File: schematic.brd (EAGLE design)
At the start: 100 x 70 mm, 33 parts, among them U1 ADP3338AKCZ-3.3RL7

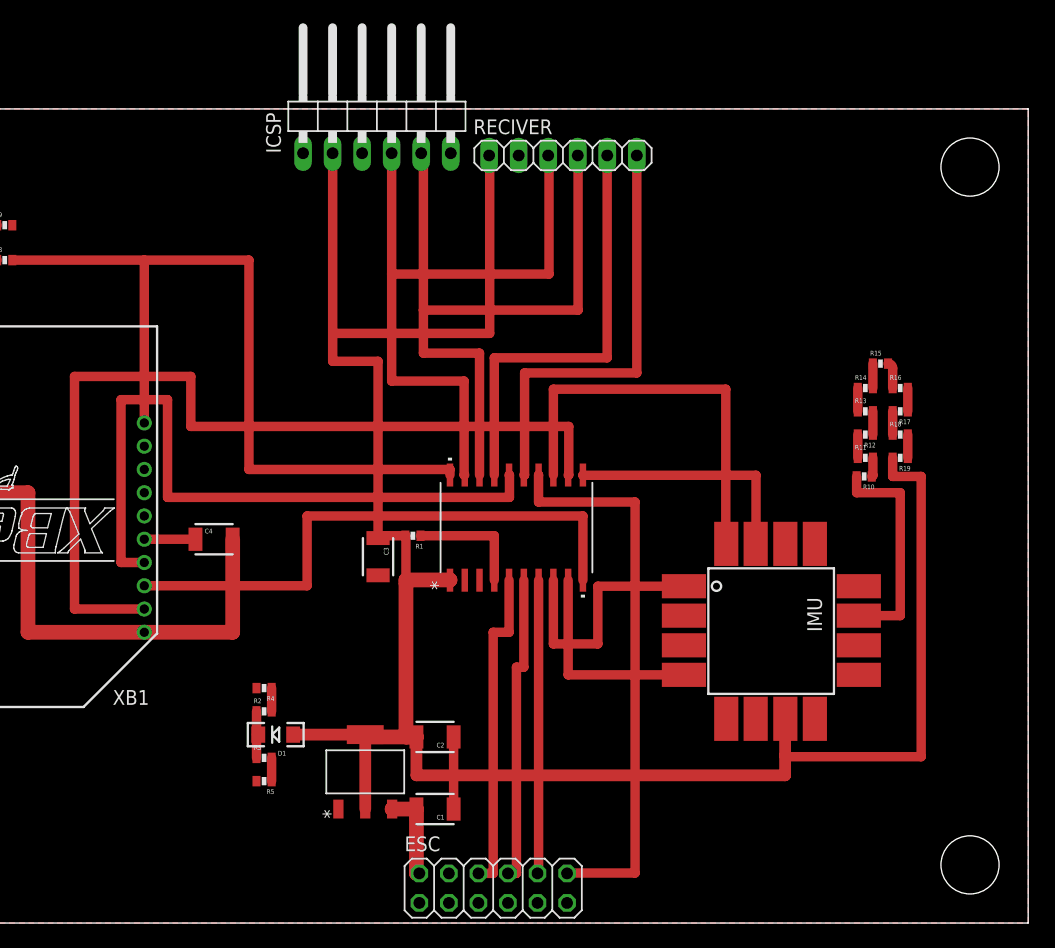
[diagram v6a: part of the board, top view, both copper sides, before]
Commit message: Added several missing components, rearanged some components to make routing easier and added last jumper cables. Board layout is theretically done now
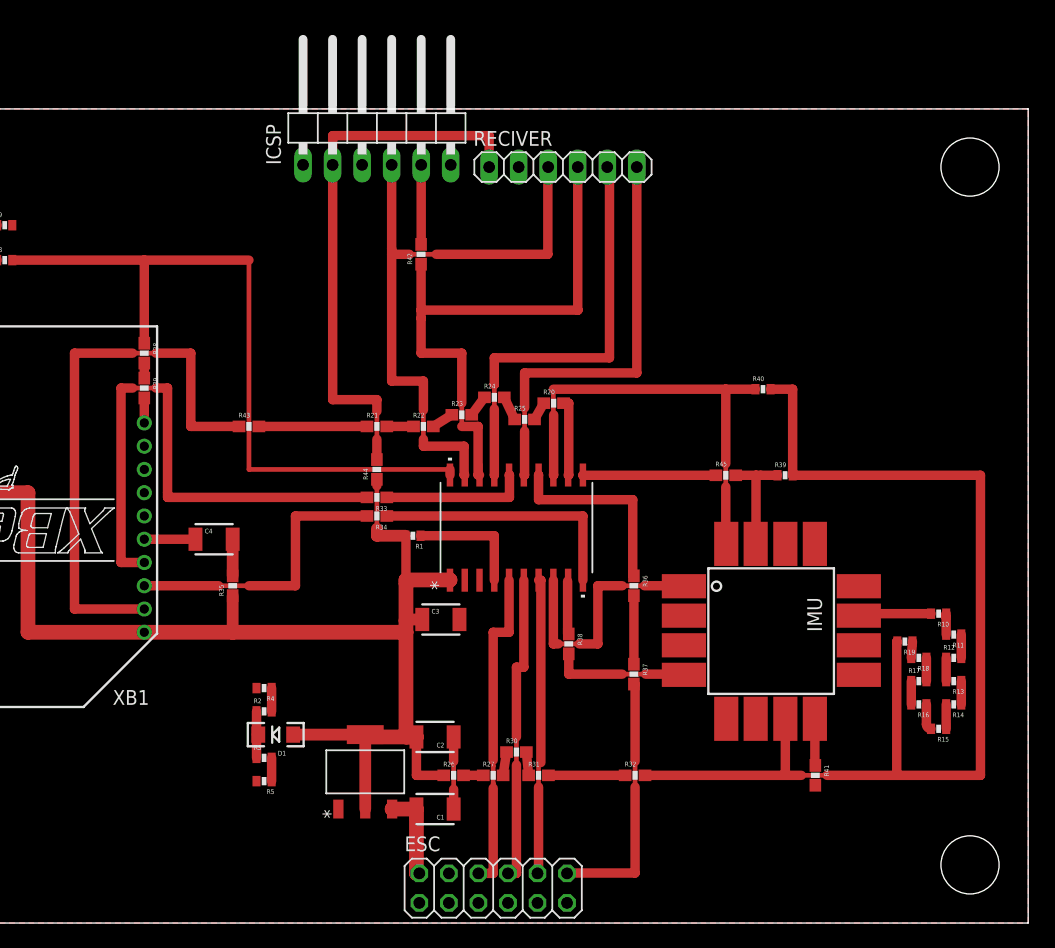
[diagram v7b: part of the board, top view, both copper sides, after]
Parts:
- added R20, R21, R22, R23, R24, R25, R26, R27, R28, R29, R30, R31, R32, R33, R34, R35, R36, R37, R38, R41, R42, R43, R44, R45: 0, SparkFun-Passives:0603-RES
- added R39, R40: 10k, SparkFun-Passives:0402-RES
- moved R15 31.8 mm to (92.3, 16.7), turned to 180 degrees
- moved R14 28.2 mm to (93.6, 18.8), turned to 180 degrees
- moved R16 27.2 mm to (90.6, 18.8), turned to 180 degrees
- moved R13 24.4 mm to (93.6, 20.8), turned to 180 degrees
- moved R17 23.3 mm to (90.6, 20.8), turned to 0 degrees
- moved R12 20.6 mm to (93.6, 22.8), turned to 0 degrees
- moved R18 19.3 mm to (90.6, 22.8), turned to 180 degrees
- moved R11 17.0 mm to (93.6, 24.8), turned to 180 degrees
- moved R19 15.8 mm to (89.4, 24.2)
- moved R10 13.4 mm to (92.3, 26.6)
- moved C3 7.64 mm to (49.5, 26.1), turned to 0 degrees
- moved ICSP 1.00 mm to (44.0, 69.0)
- moved RECIVER 1.00 mm to (60.0, 65.0)
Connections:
- removed net VCC: C4.2, XB1.1, XB1.14
- new net GND_S: R29.2, XB1.10
- new net N$1: R20.1, R25.2
- new net N$20: R21.2, R22.1
- new net N$21: R22.2, R23.1
- new net N$22: R23.2, R24.1
- new net N$23: R24.2, R25.1
- new net N$24: R28.2, R29.1
- new net N$25: MAIN_CONTROLLER.16, R33.1
- new net N$26: R26.2, R27.1
- new net N$27: R27.2, R30.1
- new net N$28: R30.2, R31.1
- new net N$29: R31.2, R32.1
- new net N$30: R34.2, XB1.3
- new net N$31: C4.2, R35.2
- new net N$32: MAIN_CONTROLLER.14, R36.1
- new net N$33: R36.2, R37.1
- new net N$34: IMU.P$4, R38.2
- new net N$35: IMU.P$8, R41.1
- new net N$36: R21.1, R43.2
- new net N$37: ICSP.5, R42.2
- new net N$38: ICSP.2, R44.2, RECIVER.1
- new net N$39: MAIN_CONTROLLER.11, R45.1
- new net RX_S: MAIN_CONTROLLER.12, R20.2
- new net VDD_S: IMU.P$7, R19.2, R32.2, R39.2, R40.2
- net GND: now also R28.1, R41.2; no longer IMU.P$8, XB1.10
- net IMU_INT: now also R38.1; no longer IMU.P$4
- net M4: now also R37.2; no longer MAIN_CONTROLLER.14
- net PGC/ROLL: now also R42.1; no longer ICSP.5
- net RX: now also R43.1; no longer MAIN_CONTROLLER.12
- net SCL: now also R39.1, R45.2; no longer MAIN_CONTROLLER.11
- net SDA: now also R40.1
- net TX: now also R34.1; no longer XB1.3
- net VDD: now also R26.1, R35.1, R44.1, XB1.1, XB1.14; no longer ICSP.2, IMU.P$7, R19.2, RECIVER.1
- net XBEE_INT: now also R33.2; no longer MAIN_CONTROLLER.16
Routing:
- net VDD_S: track 0.00 -> 96.5 mm
- net VDD: track 187.6 -> 113.5 mm
- net VCC: track 49.6 -> 0.00 mm
- net N$38: track 0.00 -> 47.8 mm
- net RX: track 77.0 -> 48.4 mm
- net TX: track 49.2 -> 22.4 mm
- net M4: track 48.4 -> 22.2 mm
- net N$30: track 0.00 -> 25.1 mm
- net N$32: track 0.00 -> 16.9 mm
- net IMU_INT: track 18.1 -> 4.65 mm
- net N$10: track 19.3 -> 6.38 mm
- net N$25: track 0.00 -> 12.5 mm
- net XBEE_INT: track 59.8 -> 47.5 mm
- net N$34: track 0.00 -> 11.7 mm
- net N$39: track 0.00 -> 11.5 mm
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
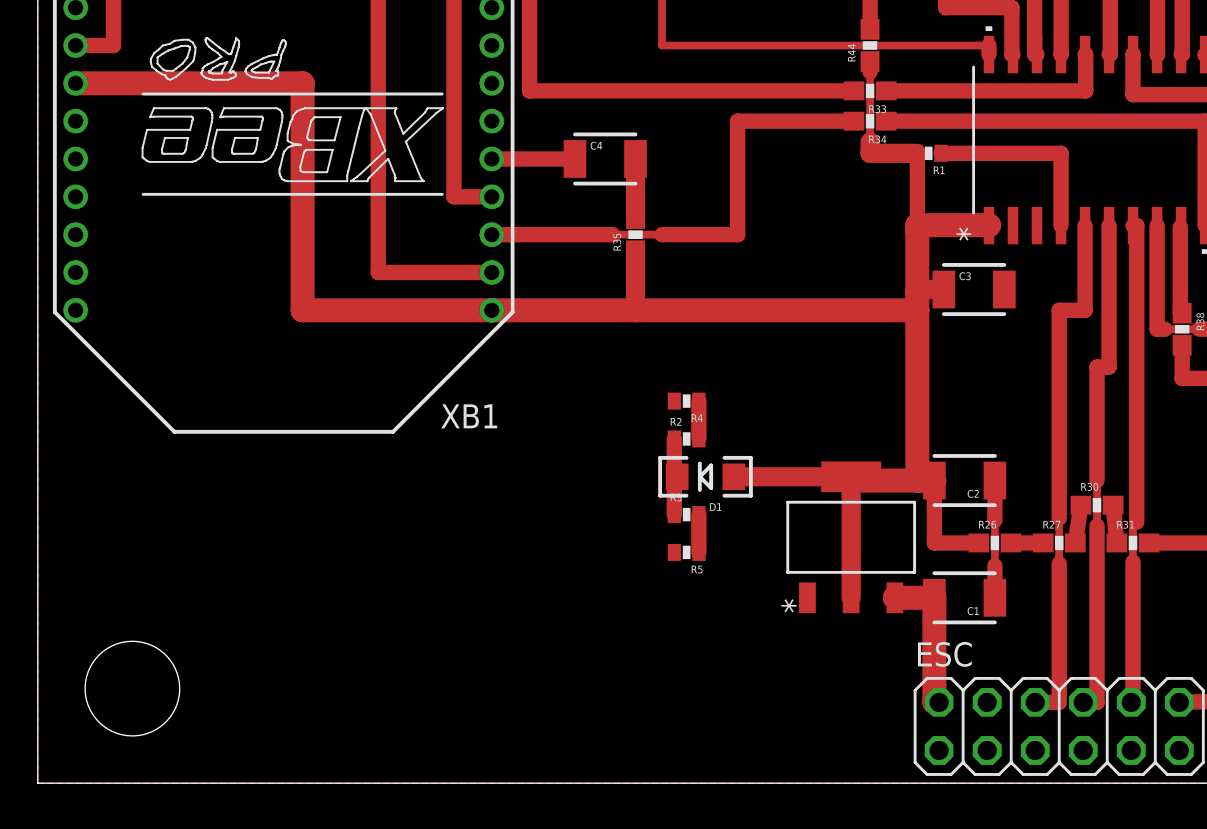
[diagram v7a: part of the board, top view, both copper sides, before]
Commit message: Rearanged several components to remove some jumper cables, added led's to unused pins on xbee and controller
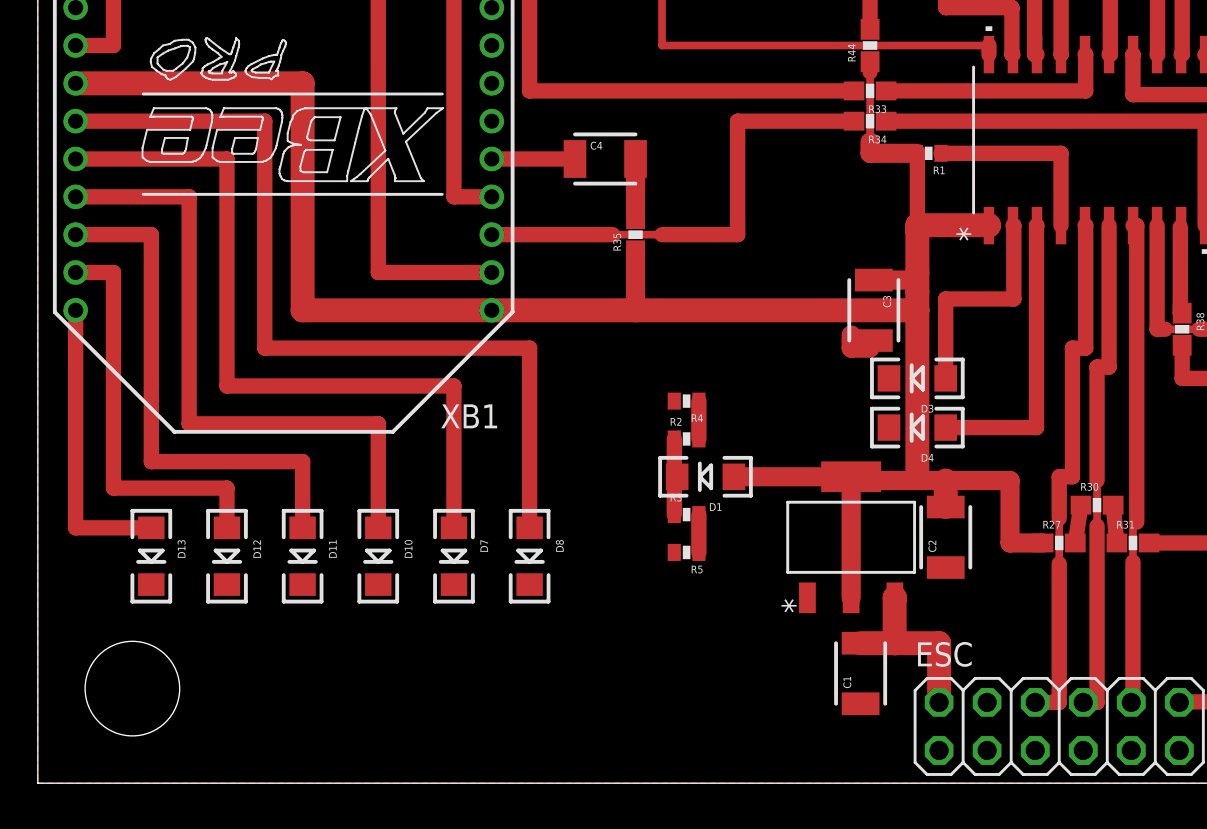
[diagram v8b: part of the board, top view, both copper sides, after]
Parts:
- removed R26: 0, SparkFun-Passives:0603-RES
- added D10, D11, D12, D13, D3, D7, D8: RED, SparkFun-LED:LED-1206
- added D4: YELLOW, SparkFun-LED:LED-1206
- moved C1 6.80 mm to (43.5, 5.80), turned to 90 degrees
- moved C3 5.41 mm to (44.2, 25.0), turned to 270 degrees
- moved C2 3.16 mm to (48.0, 13.0), turned to 90 degrees
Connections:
- removed net N$26: R26.2, R27.1
- new net N$40: D3.A, MAIN_CONTROLLER.2
- new net N$41: D4.A, MAIN_CONTROLLER.3
- new net N$43: D7.A, XB1.16
- new net N$44: D8.A, XB1.15
- new net N$45: XB1.11
- new net N$46: D10.A, XB1.17
- new net N$47: D11.A, XB1.18
- new net N$48: D12.A, XB1.19
- new net N$49: D13.A, XB1.20
- net GND: now also D10.C, D11.C, D12.C, D13.C, D3.C, D4.C, D7.C, D8.C
- net VDD: now also R27.1; no longer R26.1
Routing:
- net N$44: track 0.00 -> 45.5 mm
- net N$43: track 0.00 -> 39.5 mm
- net N$46: track 0.00 -> 33.5 mm
- net N$47: track 0.00 -> 27.5 mm
- net N$48: track 0.00 -> 21.5 mm
- net N$41: track 0.00 -> 15.5 mm
- net N$49: track 0.00 -> 15.5 mm
- net N$40: track 0.00 -> 11.7 mm
- net VDD: track 113.5 -> 118.8 mm
- net GND: track 69.1 -> 65.2 mm
- net 5V: track 7.87 -> 9.69 mm
- net N$26: track 1.70 -> 0.00 mm
